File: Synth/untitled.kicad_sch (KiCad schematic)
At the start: 9 parts, among them U1 Opamp_Dual

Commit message: added some footprints
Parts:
- C1, C2, C3, C4: footprint (none) -> Capacitor_SMD:C_0805_2012Metric
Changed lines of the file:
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@@
       (effects (font (size 1.27 1.27)) (justify left))
     )
-    (property "Footprint" "" (at 205.0542 97.917 0)
+    (property "Footprint" "Capacitor_SMD:C_0805_2012Metric" (at 205.0542 97.917 0)
       (effects (font (size 1.27 1.27)) hide)
     )
@@
       (effects (font (size 1.27 1.27)))
     )
-    (property "Footprint" "" (at 68.453 108.6358 0)
+    (property "Footprint" "Capacitor_SMD:C_0805_2012Metric" (at 68.453 108.6358 0)
       (effects (font (size 1.27 1.27)) hide)
     )
@@
       (effects (font (size 1.27 1.27)) (justify left))
     )
-    (property "Footprint" "" (at 163.9062 97.282 0)
+    (property "Footprint" "Capacitor_SMD:C_0805_2012Metric" (at 163.9062 97.282 0)
       (effects (font (size 1.27 1.27)) hide)
     )
@@
       (effects (font (size 1.27 1.27)))
     )
-    (property "Footprint" "" (at 103.378 108.6358 0)
-      (effects (font (size 1.27 1.27)) hide)
-    )
+    (property "Footprint" "Capacitor_SMD:C_0805_2012Metric" (at 103.378 108.6358 0)
+      (effects (font (size 1.27 1.27)) hide)
+    )

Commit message: add the layout
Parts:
- RV1, RV2, RV3, RV4: footprint (none) -> Potentiometer_THT:Potentiometer_Bourns_PTV09A-1_Single_Vertical
- U1: footprint (none) -> Package_TO_SOT_SMD:SC-59
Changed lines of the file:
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@@
       (effects (font (size 1.27 1.27)) (justify right))
     )
-    (property "Footprint" "" (at 72.136 116.332 0)
+    (property "Footprint" "Potentiometer_THT:Potentiometer_Bourns_PTV09A-1_Single_Vertical" (at 72.136 116.332 0)
       (effects (font (size 1.27 1.27)) hide)
     )
@@
       (effects (font (size 1.27 1.27)) (justify right))
     )
-    (property "Footprint" "" (at 107.061 116.586 0)
+    (property "Footprint" "Potentiometer_THT:Potentiometer_Bourns_PTV09A-1_Single_Vertical" (at 107.061 116.586 0)
       (effects (font (size 1.27 1.27)) hide)
     )
@@
       (effects (font (size 1.27 1.27)) (justify left))
     )
-    (property "Footprint" "" (at 114.3 56.007 0)
+    (property "Footprint" "Package_TO_SOT_SMD:SC-59" (at 114.3 56.007 0)
       (effects (font (size 1.27 1.27)) hide)
     )
@@
       (effects (font (size 1.27 1.27)))
     )
-    (property "Footprint" "" (at 193.929 87.63 0)
+    (property "Footprint" "Potentiometer_THT:Potentiometer_Bourns_PTV09A-1_Single_Vertical" (at 193.929 87.63 0)
       (effects (font (size 1.27 1.27)) hide)
     )
@@
       (effects (font (size 1.27 1.27)))
     )
-    (property "Footprint" "" (at 155.448 86.868 0)
+    (property "Footprint" "Potentiometer_THT:Potentiometer_Bourns_PTV09A-1_Single_Vertical" (at 155.448 86.868 0)
       (effects (font (size 1.27 1.27)) hide)
     )
@@
       (effects (font (size 1.27 1.27)))
     )
-    (property "Footprint" "" (at 82.931 109.601 0)
+    (property "Footprint" "Package_TO_SOT_SMD:SC-59" (at 82.931 109.601 0)
       (effects (font (size 1.27 1.27)) hide)
     )
@@
       (effects (font (size 1.27 1.27)))
     )
-    (property "Footprint" "" (at 179.578 87.63 0)
-      (effects (font (size 1.27 1.27)) hide)
-    )
+    (property "Footprint" "Package_TO_SOT_SMD:SC-59" (at 179.578 87.63 0)
+      (effects (font (size 1.27 1.27)) hide)
+    )

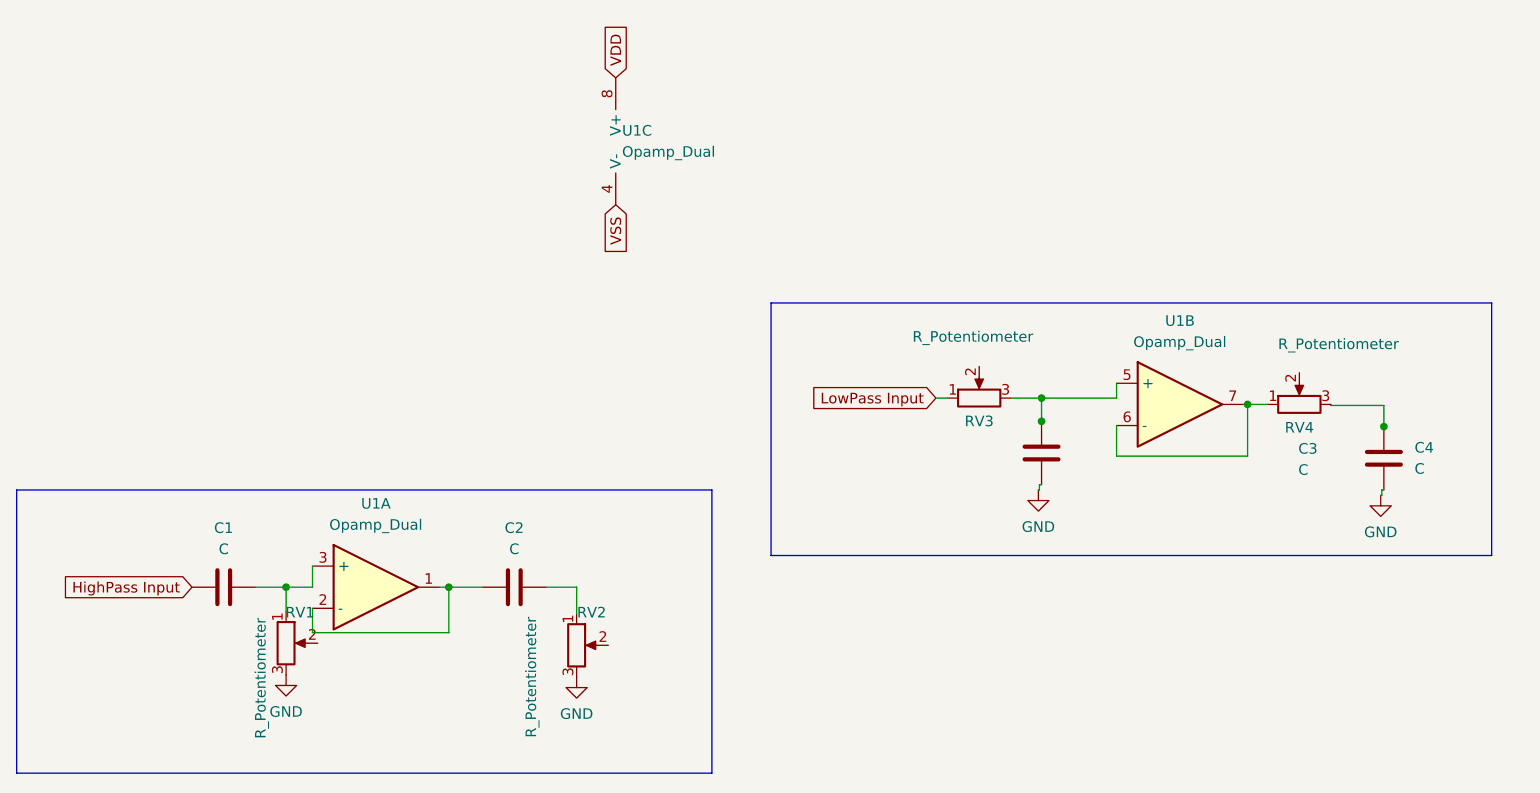
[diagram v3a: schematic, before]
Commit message: fixed erc errs
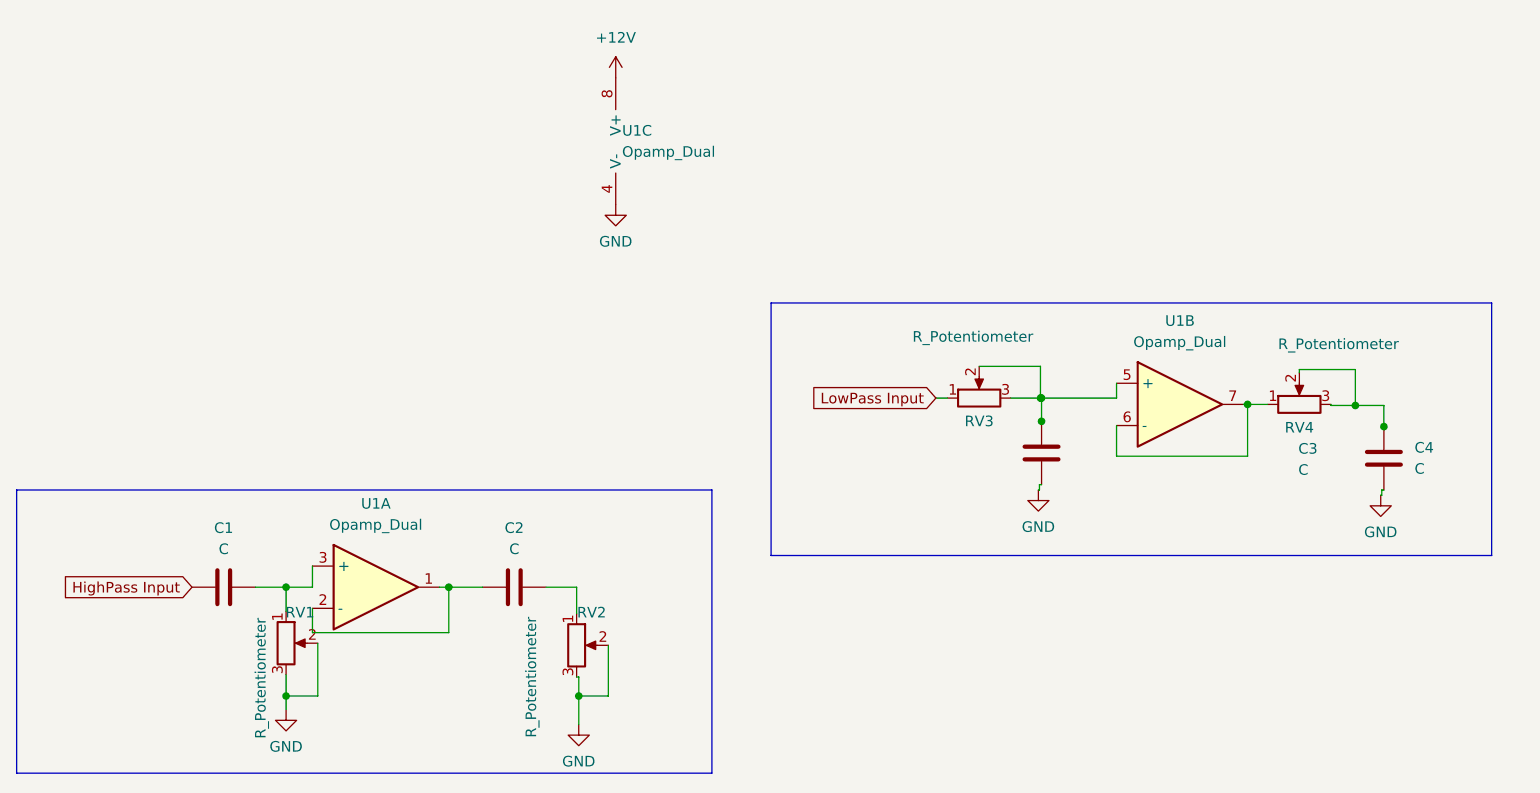
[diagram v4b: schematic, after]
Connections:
- net VSS is gone; now on net GND: U1.4 (V-)
- net GND: now also RV1.2, RV2.2
- net at C4.1, RV4.3: now also RV4.2
- net at RV3.2: now also C3.1, RV3.3, U1.5 (+)
- net VDD renamed +12V
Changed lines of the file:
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@@
   (junction (at 187.706 87.63) (diameter 0) (color 0 0 0 0)
   )
+  (junction (at 200.66 87.757) (diameter 0) (color 0 0 0 0)
+  )
+  (junction (at 72.136 122.682) (diameter 0) (color 0 0 0 0)
+  )
+  (junction (at 107.315 122.682) (diameter 0) (color 0 0 0 0)
+  )
   (junction (at 204.089 90.297) (diameter 0) (color 0 0 0 0)
   )
+  (junction (at 162.814 86.868) (diameter 0) (color 0 0 0 0)
+  )
   (junction (at 162.941 86.868) (diameter 0) (color 0 0 0 0)
   )
@@
     (stroke (width 0) (type default))
   )
+  (wire (pts (xy 162.814 86.868) (xy 162.941 86.868))
+    (stroke (width 0) (type default))
+  )
+  (wire (pts (xy 107.315 126.111) (xy 107.315 122.682))
+    (stroke (width 0) (type default))
+  )
   (wire (pts (xy 187.706 93.853) (xy 171.958 93.853))
     (stroke (width 0) (type default))
   )
+  (wire (pts (xy 200.66 87.757) (xy 204.089 87.757))
+    (stroke (width 0) (type default))
+  )
   (wire (pts (xy 162.941 97.282) (xy 162.687 97.282))
     (stroke (width 0) (type default))
   )
+  (wire (pts (xy 107.315 122.682) (xy 107.315 120.396))
+    (stroke (width 0) (type default))
+  )
   (wire (pts (xy 187.198 87.63) (xy 187.706 87.63))
     (stroke (width 0) (type default))
   )
+  (wire (pts (xy 162.814 83.058) (xy 162.814 86.868))
+    (stroke (width 0) (type default))
+  )
   (wire (pts (xy 187.706 87.63) (xy 190.119 87.63))
     (stroke (width 0) (type default))
@@
     (stroke (width 0) (type default))
   )
+  (wire (pts (xy 155.448 83.058) (xy 162.814 83.058))
+    (stroke (width 0) (type default))
+  )
   (wire (pts (xy 75.311 115.062) (xy 91.694 115.062))
     (stroke (width 0) (type default))
   )
+  (wire (pts (xy 107.315 122.682) (xy 110.871 122.682))
+    (stroke (width 0) (type default))
+  )
   (wire (pts (xy 107.061 109.601) (xy 107.061 112.776))
     (stroke (width 0) (type default))
   )
+  (wire (pts (xy 200.66 83.439) (xy 200.66 87.757))
+    (stroke (width 0) (type default))
+  )
   (wire (pts (xy 204.089 87.757) (xy 204.089 90.297))
     (stroke (width 0) (type default))
@@
     (stroke (width 0) (type default))
   )
+  (wire (pts (xy 193.929 83.439) (xy 193.929 83.82))
+    (stroke (width 0) (type default))
+  )
   (wire (pts (xy 103.378 109.601) (xy 107.061 109.601))
     (stroke (width 0) (type default))
@@
     (stroke (width 0) (type default))
   )
-  (wire (pts (xy 197.739 87.757) (xy 204.089 87.757))
+  (wire (pts (xy 197.739 87.757) (xy 200.66 87.757))
     (stroke (width 0) (type default))
   )
@@
     (stroke (width 0) (type default))
   )
+  (wire (pts (xy 107.315 120.396) (xy 107.061 120.396))
+    (stroke (width 0) (type default))
+  )
   (wire (pts (xy 91.694 109.601) (xy 91.694 115.062))
     (stroke (width 0) (type default))
@@
     (stroke (width 0) (type default))
   )
-  (wire (pts (xy 159.258 86.868) (xy 162.941 86.868))
+  (wire (pts (xy 159.258 86.868) (xy 162.814 86.868))
     (stroke (width 0) (type default))
   )
@@
     (stroke (width 0) (type default))
   )
+  (wire (pts (xy 72.136 122.682) (xy 72.136 120.142))
+    (stroke (width 0) (type default))
+  )
   (wire (pts (xy 197.739 87.63) (xy 197.739 87.757))
     (stroke (width 0) (type default))
   )
+  (wire (pts (xy 75.946 116.332) (xy 75.946 122.682))
+    (stroke (width 0) (type default))
+  )
   (wire (pts (xy 171.958 86.868) (xy 171.958 85.09))
     (stroke (width 0) (type default))
   )
+  (wire (pts (xy 110.871 116.586) (xy 110.871 122.682))
+    (stroke (width 0) (type default))
+  )
   (wire (pts (xy 72.136 109.601) (xy 75.311 109.601))
     (stroke (width 0) (type default))
   )
+  (wire (pts (xy 72.136 122.682) (xy 75.946 122.682))
+    (stroke (width 0) (type default))
+  )
   (wire (pts (xy 203.835 98.552) (xy 203.708 98.552))
     (stroke (width 0) (type default))
   )
   (wire (pts (xy 162.687 97.917) (xy 162.56 97.917))
+    (stroke (width 0) (type default))
+  )
+  (wire (pts (xy 72.136 124.333) (xy 72.136 122.682))
+    (stroke (width 0) (type default))
+  )
+  (wire (pts (xy 193.929 83.439) (xy 200.66 83.439))
     (stroke (width 0) (type default))
   )
@@
     )
   )
-  (global_label "VDD" (shape input) (at 111.76 48.387 90) (fields_autoplaced)
-    (effects (font (size 1.27 1.27)) (justify left))
-    (property "Intersheetrefs" "${INTERSHEET_REFS}" (at 111.76 41.7732 90)
-      (effects (font (size 1.27 1.27)) (justify left) hide)
-    )
-  )
   (global_label "HighPass Input" (shape input) (at 60.833 109.601 180) (fields_autoplaced)
     (effects (font (size 1.27 1.27)) (justify right))
@@
     )
   )
-  (global_label "VSS" (shape input) (at 111.76 63.627 270) (fields_autoplaced)
-    (effects (font (size 1.27 1.27)) (justify right))
-    (property "Intersheetrefs" "${INTERSHEET_REFS}" (at 111.76 70.1198 90)
-      (effects (font (size 1.27 1.27)) (justify right) hide)
-    )
-  )
   (symbol (lib_id "Device:R_Potentiometer") (at 72.136 116.332 0) (unit 1)
     (in_bom yes) (on_board yes) (dnp no)
@@
     )
   )
-  (symbol (lib_id "power:GND") (at 107.061 120.396 0) (unit 1)
-    (in_bom yes) (on_board yes) (dnp no) (fields_autoplaced)
-    (property "Reference" "#PWR02" (at 107.061 126.746 0)
-      (effects (font (size 1.27 1.27)) hide)
-    )
-    (property "Value" "GND" (at 107.061 124.841 0)
-      (effects (font (size 1.27 1.27)))
-    )
-    (property "Footprint" "" (at 107.061 120.396 0)
-      (effects (font (size 1.27 1.27)) hide)
-    )
-    (property "Datasheet" "" (at 107.061 120.396 0)
+  (symbol (lib_id "power:GND") (at 107.315 126.111 0) (unit 1)
+    (in_bom yes) (on_board yes) (dnp no) (fields_autoplaced)
+    (property "Reference" "#PWR02" (at 107.315 132.461 0)
+      (effects (font (size 1.27 1.27)) hide)
+    )
+    (property "Value" "GND" (at 107.315 130.556 0)
+      (effects (font (size 1.27 1.27)))
+    )
+    (property "Footprint" "" (at 107.315 126.111 0)
+      (effects (font (size 1.27 1.27)) hide)
+    )
+    (property "Datasheet" "" (at 107.315 126.111 0)
       (effects (font (size 1.27 1.27)) hide)
     )
@@
     )
   )
+  (symbol (lib_id "power:+12V") (at 111.76 48.387 0) (mirror y) (unit 1)
+    (in_bom yes) (on_board yes) (dnp no) (fields_autoplaced)
+    (property "Reference" "#PWR037" (at 111.76 52.197 0)
+      (effects (font (size 1.27 1.27)) hide)
+    )
+    (property "Value" "+12V" (at 111.76 43.561 0)
+      (effects (font (size 1.27 1.27)))
+    )
+    (property "Footprint" "" (at 111.76 48.387 0)
+      (effects (font (size 1.27 1.27)) hide)
+    )
+    (property "Datasheet" "" (at 111.76 48.387 0)
+      (effects (font (size 1.27 1.27)) hide)
+    )
+    (pin "1")
+    (instances
+      (project "Synth"
+        (path "/69caad27-d98a-4cdc-abd0-794bd5e6ba79/992b309c-40d2-4352-97b7-0477e3977f90"
+          (reference "#PWR037") (unit 1)
+        )
+      )
+    )
+  )
   (symbol (lib_id "Device:C") (at 64.643 109.601 90) (unit 1)
     (in_bom yes) (on_board yes) (dnp no) (fields_autoplaced)
@@
     )
   )
+  (symbol (lib_id "power:GND") (at 111.76 63.627 0) (unit 1)
+    (in_bom yes) (on_board yes) (dnp no) (fields_autoplaced)
+    (property "Reference" "#PWR036" (at 111.76 69.977 0)
+      (effects (font (size 1.27 1.27)) hide)
+    )
+    (property "Value" "GND" (at 111.76 68.072 0)
+      (effects (font (size 1.27 1.27)))
+    )
+    (property "Footprint" "" (at 111.76 63.627 0)
+      (effects (font (size 1.27 1.27)) hide)
+    )
+    (property "Datasheet" "" (at 111.76 63.627 0)
+      (effects (font (size 1.27 1.27)) hide)
+    )
+    (pin "1")
+    (instances
+      (project "Synth"
+        (path "/69caad27-d98a-4cdc-abd0-794bd5e6ba79/992b309c-40d2-4352-97b7-0477e3977f90"
+          (reference "#PWR036") (unit 1)
+        )
+      )
+    )
+  )
   (symbol (lib_id "Device:C") (at 162.941 93.472 0) (unit 1)
     (in_bom yes) (on_board yes) (dnp no)
@@
     )
   )
-  (symbol (lib_id "power:GND") (at 72.136 120.142 0) (unit 1)
-    (in_bom yes) (on_board yes) (dnp no) (fields_autoplaced)
-    (property "Reference" "#PWR01" (at 72.136 126.492 0)
-      (effects (font (size 1.27 1.27)) hide)
-    )
-    (property "Value" "GND" (at 72.136 124.587 0)
-      (effects (font (size 1.27 1.27)))
-    )
-    (property "Footprint" "" (at 72.136 120.142 0)
-      (effects (font (size 1.27 1.27)) hide)
-    )
-    (property "Datasheet" "" (at 72.136 120.142 0)
-      (effects (font (size 1.27 1.27)) hide)
-    )
+  (symbol (lib_id "power:GND") (at 72.136 124.333 0) (unit 1)
+    (in_bom yes) (on_board yes) (dnp no) (fields_autoplaced)
+    (property "Reference" "#PWR01" (at 72.136 130.683 0)
+      (effects (font (size 1.27 1.27)) hide)
+    )
+    (property "Value" "GND" (at 72.136 128.778 0)
+      (effects (font (size 1.27 1.27)))
+    )
+    (property "Footprint" "" (at 72.136 124.333 0)
+      (effects (font (size 1.27 1.27)) hide)
+    )
+    (property "Datasheet" "" (at 72.136 124.333 0)
+      (effects (font (size 1.27 1.27)) hide)
+    )

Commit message: add the ESP
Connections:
- net LowPass Input: now also C2.2, RV2.1
- net Filter Out: now reaches C4.1, RV4.2, RV4.3
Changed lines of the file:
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@@
     (fill (type none))
+  )
+  (global_label "LowPass Input" (shape input) (at 107.061 109.601 0) (fields_autoplaced)
+    (effects (font (size 1.27 1.27)) (justify left))
+    (property "Intersheetrefs" "${INTERSHEET_REFS}" (at 123.7741 109.601 0)
+      (effects (font (size 1.27 1.27)) (justify left) hide)
+    )
   )
   (global_label "LowPass Input" (shape input) (at 150.241 86.868 180) (fields_autoplaced)
@@
     )
   )
+  (global_label "Filter Out" (shape input) (at 204.089 87.884 0) (fields_autoplaced)
+    (effects (font (size 1.27 1.27)) (justify left))
+    (property "Intersheetrefs" "${INTERSHEET_REFS}" (at 216.2061 87.884 0)
+      (effects (font (size 1.27 1.27)) (justify left) hide)
+    )
+  )

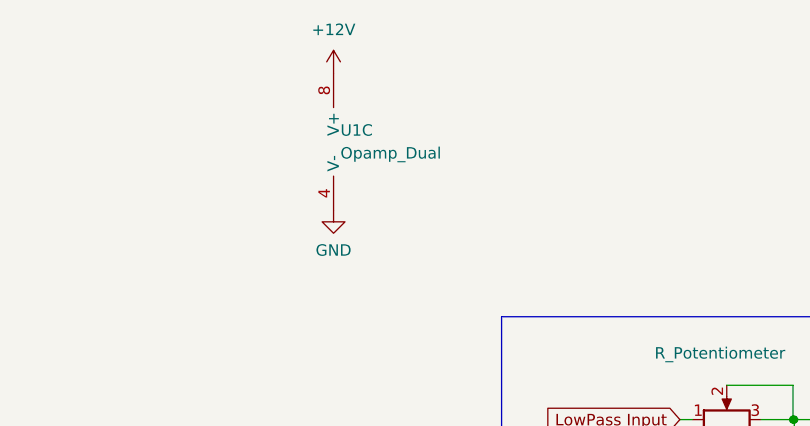
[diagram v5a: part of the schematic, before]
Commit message: changed the potentiometer footprints
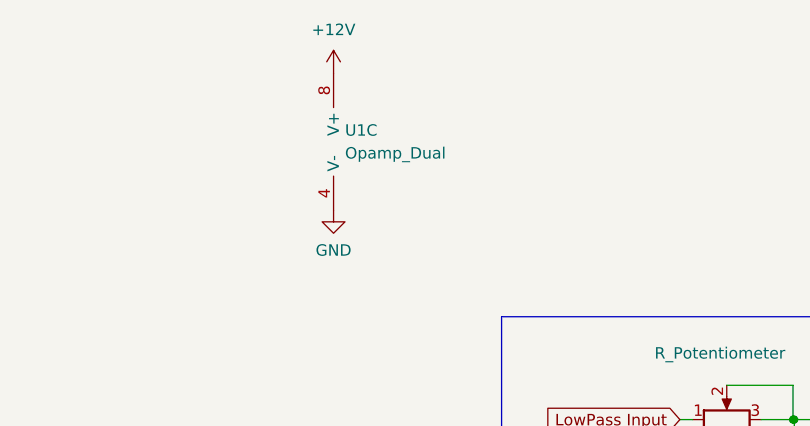
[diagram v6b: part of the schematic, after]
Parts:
- RV1, RV2, RV3, RV4: footprint Potentiometer_THT:Potentiometer_Bourns_PTV09A-1_Single_Vertical -> Potentiometer_THT:Potentiometer_Bourns_3299W_Vertical
- U1: footprint Package_TO_SOT_SMD:SC-59 -> Package_TO_SOT_SMD:TSOT-23-8
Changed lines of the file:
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@@
       (effects (font (size 1.27 1.27)) (justify right))
     )
-    (property "Footprint" "Potentiometer_THT:Potentiometer_Bourns_PTV09A-1_Single_Vertical" (at 72.136 116.332 0)
+    (property "Footprint" "Potentiometer_THT:Potentiometer_Bourns_3299W_Vertical" (at 72.136 116.332 0)
       (effects (font (size 1.27 1.27)) hide)
     )
@@
       (effects (font (size 1.27 1.27)) (justify right))
     )
-    (property "Footprint" "Potentiometer_THT:Potentiometer_Bourns_PTV09A-1_Single_Vertical" (at 107.061 116.586 0)
+    (property "Footprint" "Potentiometer_THT:Potentiometer_Bourns_3299W_Vertical" (at 107.061 116.586 0)
       (effects (font (size 1.27 1.27)) hide)
     )
@@
   (symbol (lib_id "Device:Opamp_Dual") (at 114.3 56.007 0) (unit 3)
     (in_bom yes) (on_board yes) (dnp no) (fields_autoplaced)
-    (property "Reference" "U1" (at 112.522 54.737 0)
+    (property "Reference" "U1" (at 113.03 54.737 0)
       (effects (font (size 1.27 1.27)) (justify left))
     )
-    (property "Value" "Opamp_Dual" (at 112.522 57.277 0)
+    (property "Value" "Opamp_Dual" (at 113.03 57.277 0)
       (effects (font (size 1.27 1.27)) (justify left))
     )
-    (property "Footprint" "Package_TO_SOT_SMD:SC-59" (at 114.3 56.007 0)
+    (property "Footprint" "Package_TO_SOT_SMD:TSOT-23-8" (at 114.3 56.007 0)
       (effects (font (size 1.27 1.27)) hide)
     )
@@
       (effects (font (size 1.27 1.27)))
     )
-    (property "Footprint" "Potentiometer_THT:Potentiometer_Bourns_PTV09A-1_Single_Vertical" (at 193.929 87.63 0)
+    (property "Footprint" "Potentiometer_THT:Potentiometer_Bourns_3299W_Vertical" (at 193.929 87.63 0)
       (effects (font (size 1.27 1.27)) hide)
     )
@@
       (effects (font (size 1.27 1.27)))
     )
-    (property "Footprint" "Potentiometer_THT:Potentiometer_Bourns_PTV09A-1_Single_Vertical" (at 155.448 86.868 0)
+    (property "Footprint" "Potentiometer_THT:Potentiometer_Bourns_3299W_Vertical" (at 155.448 86.868 0)
       (effects (font (size 1.27 1.27)) hide)
     )
@@
       (effects (font (size 1.27 1.27)))
     )
-    (property "Footprint" "Package_TO_SOT_SMD:SC-59" (at 82.931 109.601 0)
+    (property "Footprint" "Package_TO_SOT_SMD:TSOT-23-8" (at 82.931 109.601 0)
       (effects (font (size 1.27 1.27)) hide)
     )
@@
       (effects (font (size 1.27 1.27)))
     )
-    (property "Footprint" "Package_TO_SOT_SMD:SC-59" (at 179.578 87.63 0)
-      (effects (font (size 1.27 1.27)) hide)
-    )
+    (property "Footprint" "Package_TO_SOT_SMD:TSOT-23-8" (at 179.578 87.63 0)
+      (effects (font (size 1.27 1.27)) hide)
+    )
